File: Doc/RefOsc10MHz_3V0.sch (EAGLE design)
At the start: 58 parts, among them CON1 SD-73100-0105, CON10 MCX-J-P-X-RA-SM1, CON2 TYCO-AMP_USBUSB-B_SMT, CON3 MCX-J-P-X-RA-SM1, CON4 AVR-ISP-6SMD, CON5 AVR-JTAG-10SMD, CON6 HEADER-2X3SMD, CON7 MCX-J-P-X-RA-SM1, CON8 MCX-J-P-X-RA-SM1, CON9 MCX-J-P-X-RA-SM1, IC11 712-RXM-GNSS-TM-B, IC3 74HCT221D, IC4 CFPT-141, U1 6SLX4TQG144

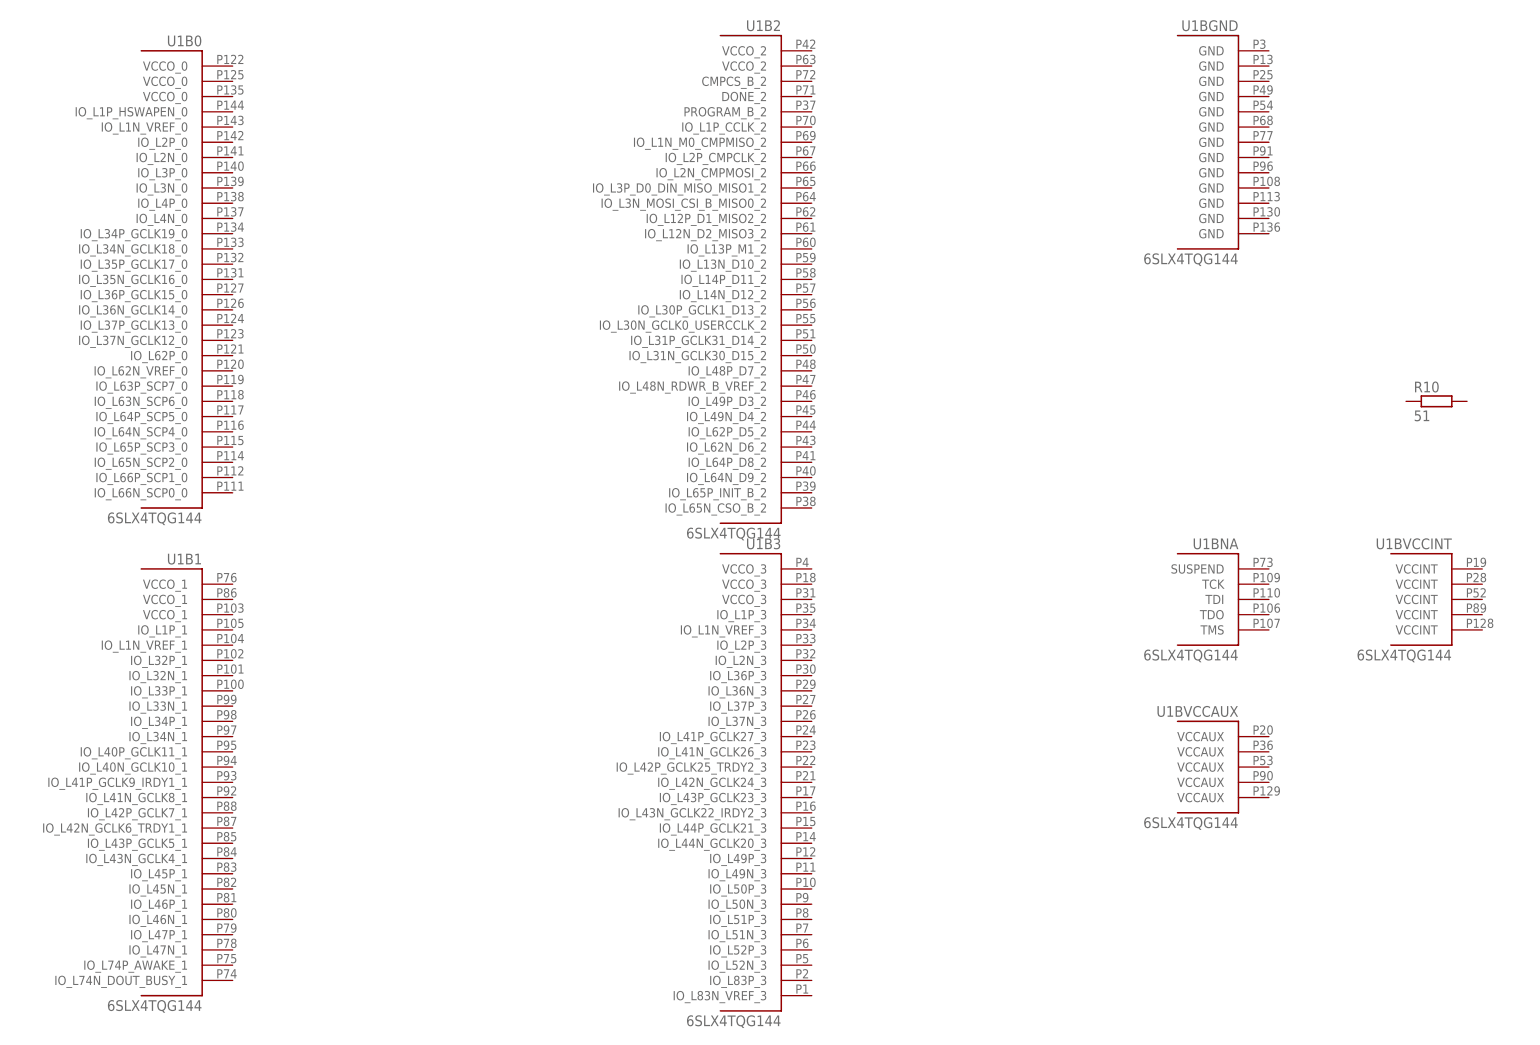
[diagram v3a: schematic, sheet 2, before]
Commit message: avr_DF4IAH_Bootloader - Doc - Eagle: V3.0 - xilinx_devices_V6.lbr containing XC7-Artix added (2)
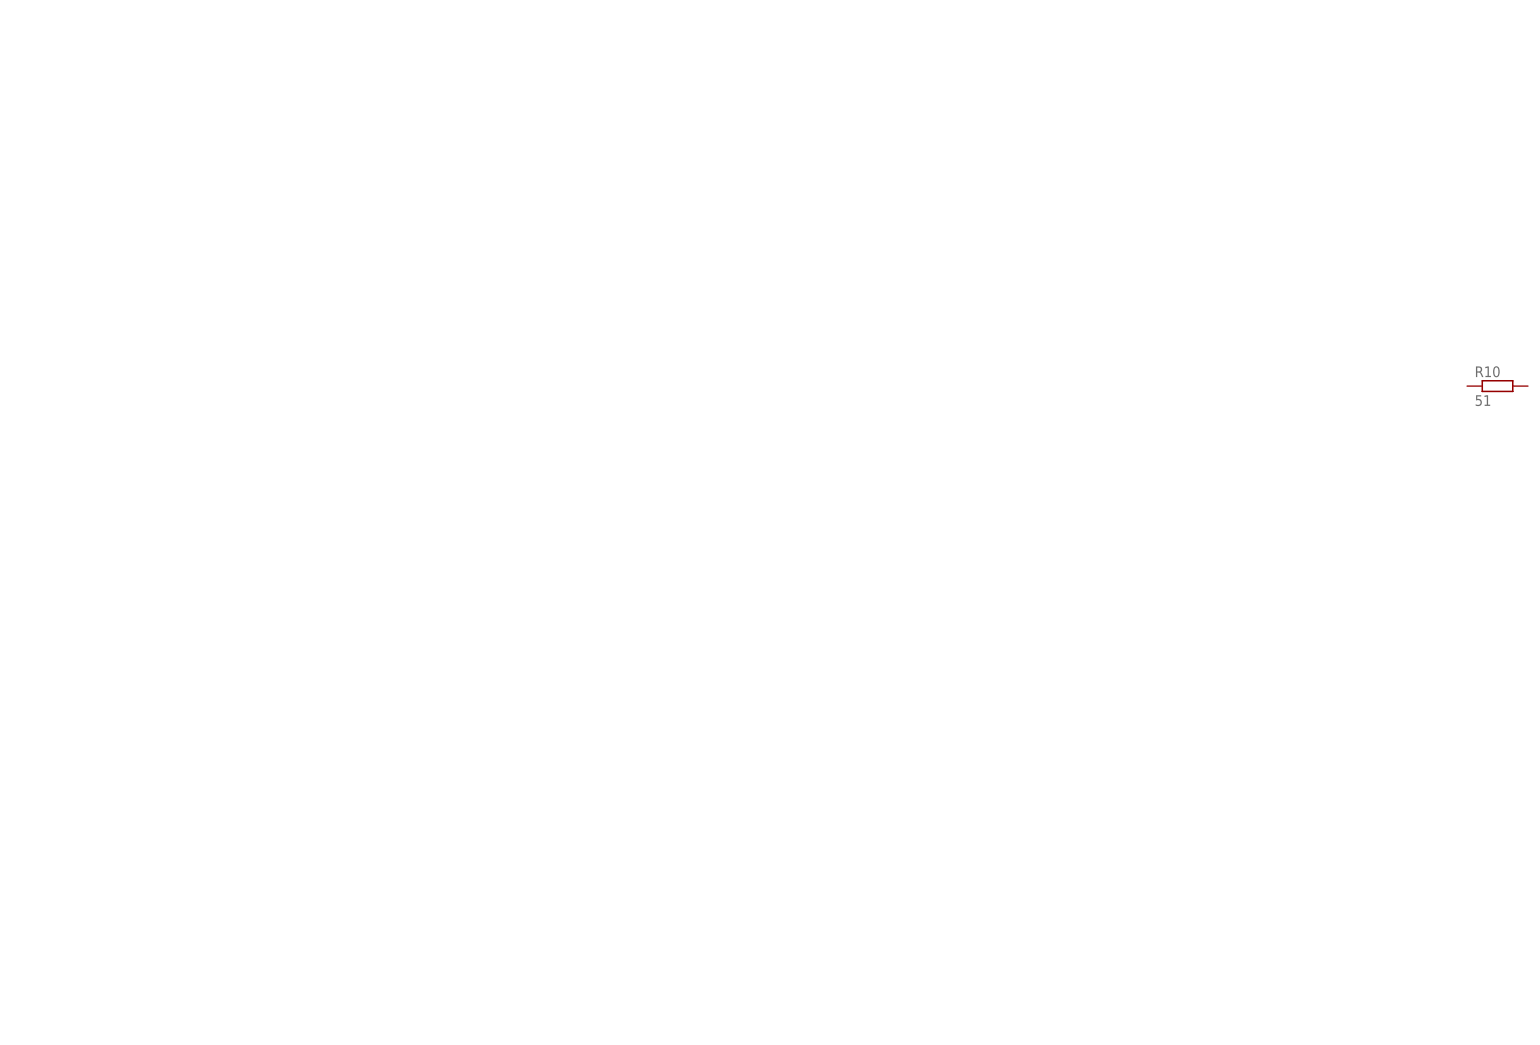
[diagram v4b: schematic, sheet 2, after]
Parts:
- removed U1: 6SLX4TQG144, xilinx_devices_V6:6SLX4TQG144
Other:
- moved on the sheet: R10
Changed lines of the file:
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@@
 <part name="CON10" library="df4iah" deviceset="MCX-J-P-X-RA-SM1" device=""/>
 <part name="R10" library="rcl" deviceset="R-EU_" device="R0805" value="51"/>
-<part name="U1" library="xilinx_devices_V6" deviceset="6SLX4TQG144" device=""/>
 <part name="FRAME10" library="frames" deviceset="A5L-LOC" device=""/>
 <part name="FRAME12" library="frames" deviceset="A5L-LOC" device=""/>
@@
 <instances>
 <instance part="FRAME3" gate="G$1" x="0" y="7.62"/>
-<instance part="R10" gate="G$1" x="238.76" y="116.84"/>
-<instance part="U1" gate="B0" x="33.02" y="137.16"/>
-<instance part="U1" gate="B1" x="33.02" y="53.34"/>
-<instance part="U1" gate="B2" x="129.54" y="137.16"/>
-<instance part="U1" gate="B3" x="129.54" y="53.34"/>
-<instance part="U1" gate="BGND" x="205.74" y="160.02"/>
-<instance part="U1" gate="BNA" x="205.74" y="83.82"/>
-<instance part="U1" gate="BVCCAUX" x="205.74" y="55.88"/>
-<instance part="U1" gate="BVCCINT" x="241.3" y="83.82"/>
+<instance part="R10" gate="G$1" x="248.92" y="119.38"/>
 </instances>
 <busses>
